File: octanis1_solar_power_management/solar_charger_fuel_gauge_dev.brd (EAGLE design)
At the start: 100 x 58.4 mm, 14 parts, among them IC1 MSP430FW42IP, U1 BQ24210_DQC_10

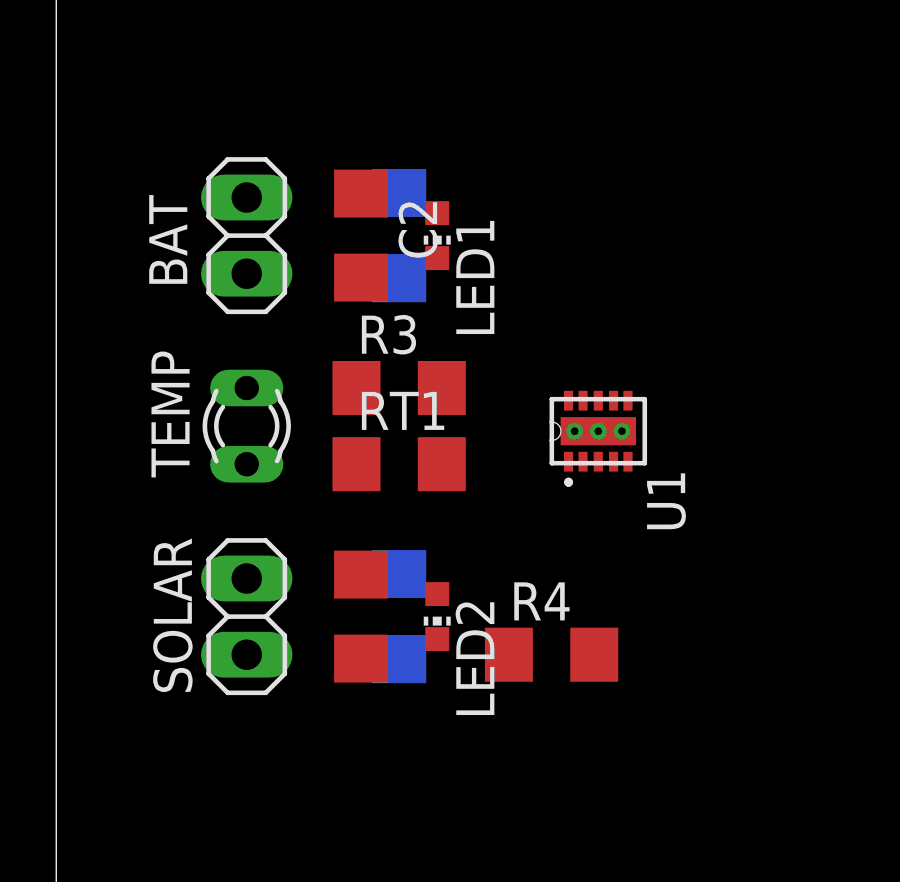
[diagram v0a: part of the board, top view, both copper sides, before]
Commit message: Completed Routing for Battery charging Part
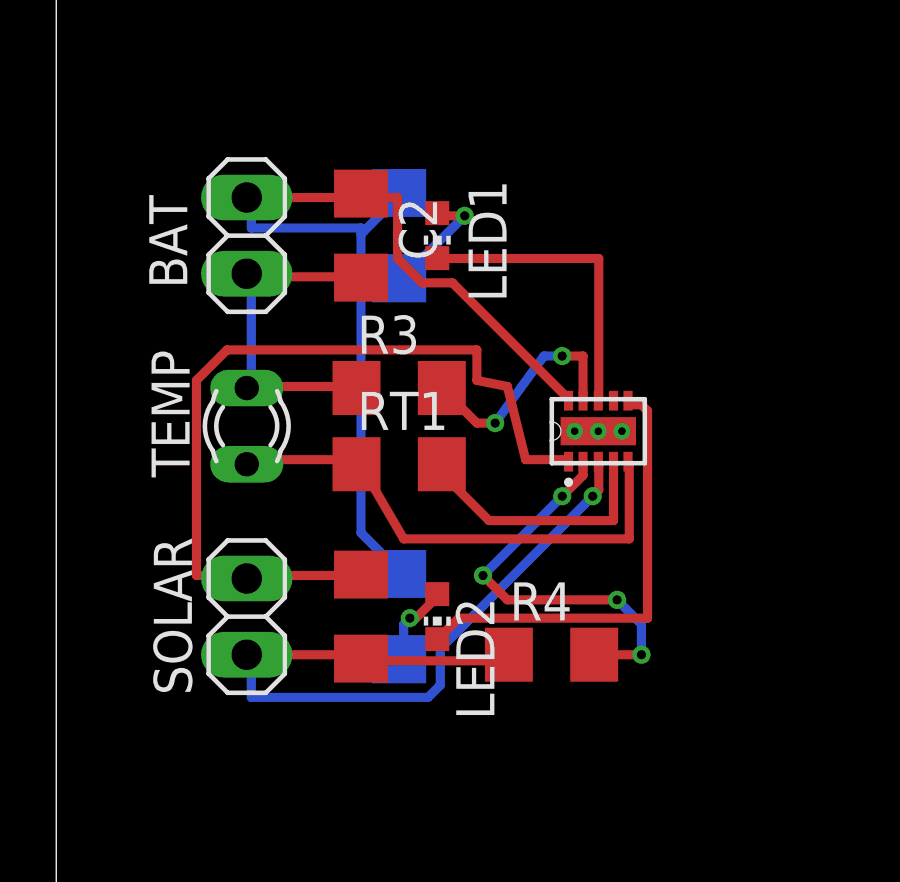
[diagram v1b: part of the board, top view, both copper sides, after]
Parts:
- U1: value BQ24210_DQC_10 -> BQ24210
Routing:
- net N$1: track 0.00 -> 33.6 mm
- net N$13: track 0.00 -> 27.9 mm
- net SOLAR: track 0.00 -> 26.7 mm, vias 0 -> 1
- net N$7: track 0.00 -> 16.9 mm
- net N$5: track 0.00 -> 15.0 mm
- net N$10: track 0.00 -> 13.7 mm, vias 0 -> 4
- net GND: track 0.00 -> 11.6 mm
- net N$4: track 0.00 -> 10.1 mm
- net N$8: track 0.00 -> 8.65 mm
- net N$6: track 0.00 -> 7.82 mm, vias 0 -> 2
- net N$2: track 0.00 -> 3.98 mm, vias 0 -> 1
- net N$3: track 0.00 -> 2.80 mm, vias 0 -> 1

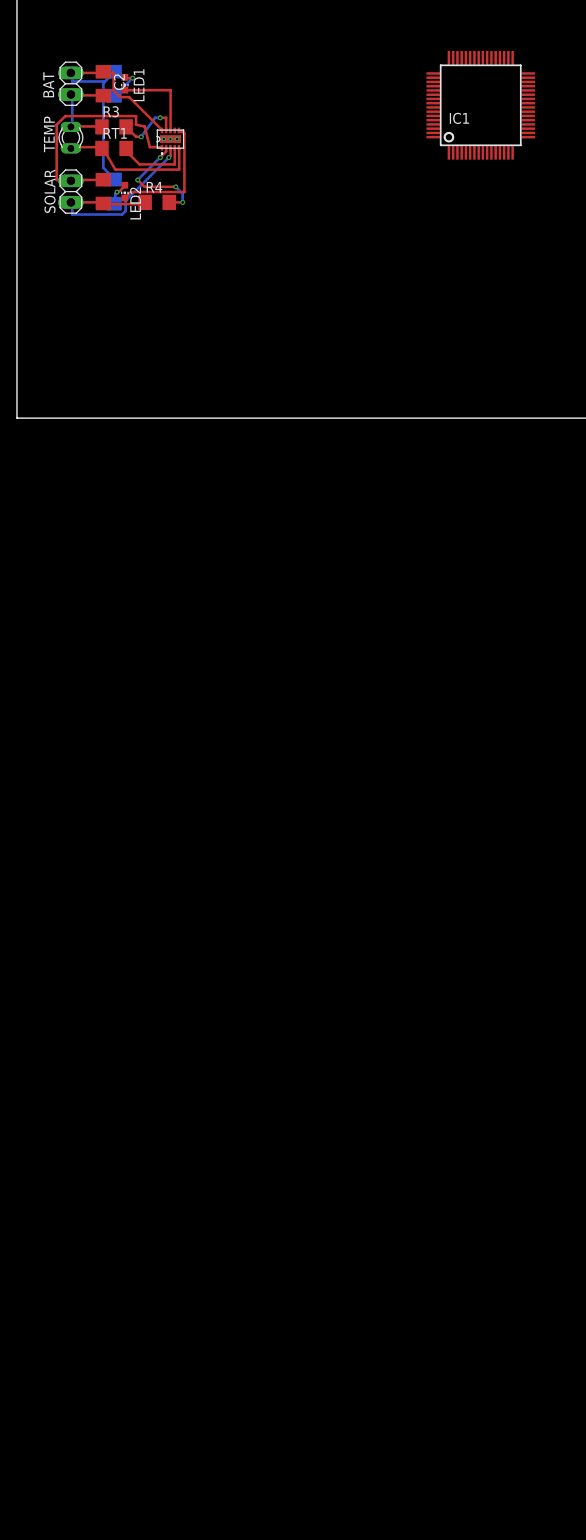
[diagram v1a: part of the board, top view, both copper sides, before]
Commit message: Added the correct MSP430 microcontroller with example circuit from LaunchPad DevBrd
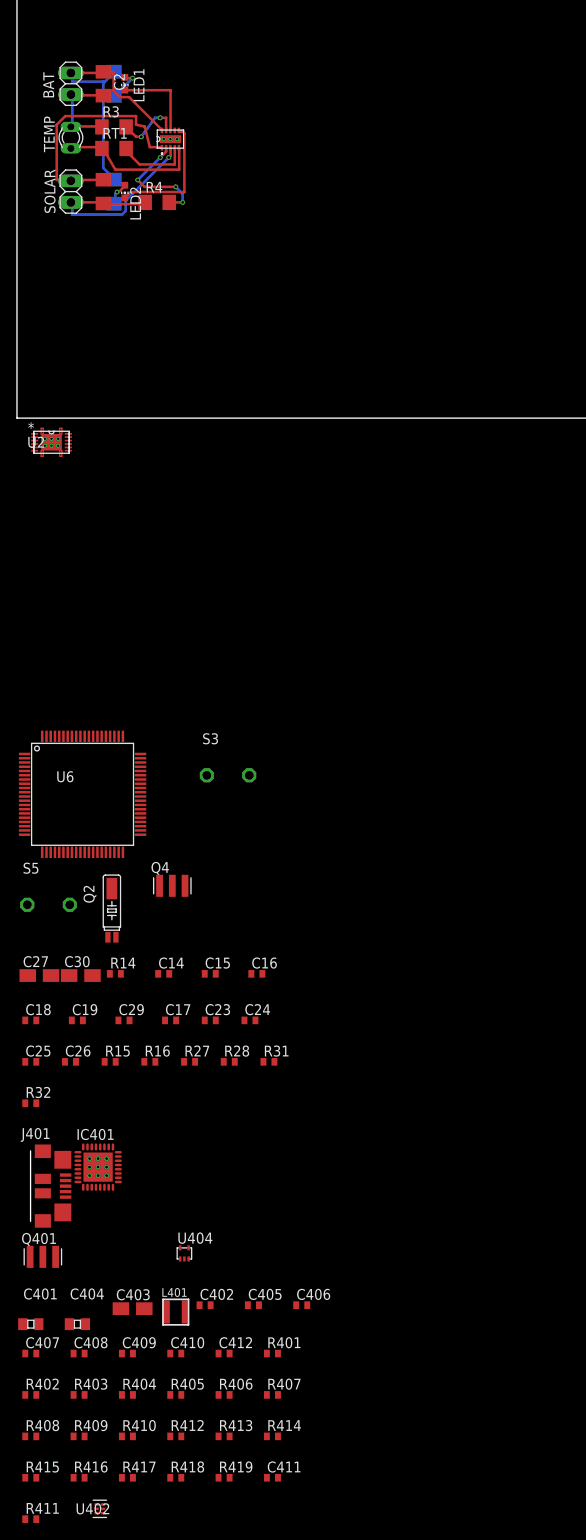
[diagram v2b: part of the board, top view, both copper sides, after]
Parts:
- removed IC1: MSP430FW42IP, texas:SQFP-S-10X10-64
- added C14, C19, C29, C402, C407, C408: 100n, rcl:C0402
- added C15, C16: 220n, rcl:C0402
- added C17: 1n, rcl:C0402
- added C18: 470n, rcl:C0402
- added C23, C24: 10p, rcl:C0402
- added C25, C26: 12p, rcl:C0402
- added C27, C403: 4u7, rcl:A/3216-18R
- added C30: 10u, rcl:A/3216-18R
- added C401, C404: 1u, CAP:CSMD0805
- added C405, C406, C409, C410, C411, C412: 22p, rcl:C0402
- added IC401: TUSB2046BIRHBIRHB, texas:RHB_S-PQFP-N32
- added J401: (no value), usb_con-update:HIROSE-ZX62R-B-5P
- added L401: 2.2uH (NR3010T2R2M), MSP-EXP430F5659:L-NR3010
- added Q2: 32.768kHz, microcrystal:MS3V-T1R
- added Q4: CSTCR4M00G15L99, murata:MURATA-FILTER_CSTCR
- added Q401: CSTCR6M00G15L99, murata:MURATA-FILTER_CSTCR
- added R14: 100R, rcl:R0402
- added R15: 1k4, rcl:R0402
- added R16: 1M, rcl:R0402
- added R27, R404: 47k, rcl:R0402
- added R28: 0R, rcl:R0402
- added R31, R32: 27R, rcl:R0402
- added R401: 33R, rcl:R0402
- added R402: 10k, rcl:R0402
- added R403, R407: 1k5, rcl:R0402
- added R405, R406, R410, R411, R416, R417: 22R, rcl:R0402
- added R408, R409, R412, R413, R414, R415, R418, R419: 15k, rcl:R0402
- added S3: RST, electricalmeter:PBTH
- added S5: BSL, electricalmeter:PBTH
- added U2: BQ27510_DRZ_12, bq27510_drz_12:DRZ12_1P95X2P45
- added U402: TPS62237DRY, tps62231dry:DRY6
- added U404: TPD2E001DRLR, Project7264:TPD2E001-DRL
- added U6: MSP430F5529IPNR, TI_MSP430_v16_intern:PN80
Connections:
- removed net AVSS: IC1.62
- removed net DVCC: IC1.1
- removed net DVSS: IC1.63
- new net !OC: IC401.10, IC401.14, IC401.18, IC401.22, R402.2
- new net !PWRON: IC401.13, IC401.17, IC401.21, IC401.9
- new net +3V3: C14.1, C19.2, C30.+, R27.2, R28.2, S5.1, U6.18, U6.50
- new net +5V: C27.+, U6.65
- new net EZFET_VBUS: C402.1, C403.+, C404.2, J401.VBUS, U402.3, U402.5, U404.1
- new net EZFET_VCC: C401.2, C407.1, IC401.25, IC401.26, IC401.3, IC401.6, IC401.8, L401.P$2, R402.1, R403.1, R404.1, U402.6
- new net HUB_DM1: R31.1, R416.2, R419.1
- new net HUB_DM2: R410.2, R415.1
- new net HUB_DP1: R32.1, R417.2, R418.1
- new net HUB_DP2: R411.2, R414.1
- new net N$14: R14.1, S5.2
- new net N$15: J401.SHIELD1, R401.1
- new net N$16: J401.D+, R405.2, U404.5
- new net N$17: J401.D-, R406.2, U404.3
- new net N$18: C406.1, IC401.2, R406.1
- new net N$19: C405.1, IC401.1, R403.2, R405.1
- new net N$20: C412.1, IC401.11, R416.1
- new net N$21: C411.1, IC401.12, R417.1
- new net N$22: C409.1, IC401.16, R411.1
- new net N$23: C410.1, IC401.15, R410.1
- new net N$24: L401.P$1, U402.2
- new net N$25: IC401.29, R407.2
- new net N$26: C408.1, IC401.4, R404.2
- new net N$27: IC401.24, R408.2
- new net N$28: IC401.23, R409.2
- new net N$29: IC401.20, R412.2
- new net N$30: IC401.19, R413.2
- new net N$31: Q401.3, R407.1
- new net N$32: IC401.30, Q401.1
- new net P1.0: U6.21
- new net P1.1: U6.22
- new net P1.2: U6.23
- new net P1.3: U6.24
- new net P1.4: U6.25
- new net P1.5: U6.26
- new net P1.6: U6.27
- new net P1.7: U6.28
- new net P2.0: U6.29
- new net P2.1: U6.30
- new net P2.2: U6.31
- new net P2.3: U6.32
- new net P2.4: U6.33
- new net P2.5: U6.34
- new net P2.6: U6.35
- new net P2.7: U6.36
- new net P3.0: U6.37
- new net P3.1: U6.38
- new net P3.2: U6.39
- new net P3.3: U6.40
- new net P3.4: U6.41
- new net P3.5: U6.42
- new net P3.6: U6.43
- new net P3.7: U6.44
- new net P4.0: U6.45
- new net P4.1: U6.46
- new net P4.2: U6.47
- new net P4.3: U6.48
- new net P4.4/UCA1TXD: U6.51
- new net P4.5/UCA1RXD: U6.52
- new net P4.7: U6.54
- new net P5.2/XT2IN: Q4.3, U6.69
- new net P5.3/XT2OUT: Q4.1, U6.70
- new net P5.4/XIN: C26.2, Q2.P2, U6.12
- new net P5.5/XOUT: C25.2, Q2.P1, U6.13
- new net P6.0: U6.77
- new net P6.1: U6.78
- new net P6.2: U6.79
- new net P6.3: U6.80
- new net P6.4: U6.1
- new net P6.5: U6.2
- new net P6.6: U6.3
- new net P6.7: U6.4
- new net P7.0: U6.5
- new net P7.4: U6.57
- new net P8.1: U6.16
- new net P8.2: U6.17
- new net REG25: U2.2
- new net REGIN: U2.3
- new net RST/SBWTDIO: C17.1, R27.1, S3.2, U6.76
- new net TARGET_DM: C24.1, R31.2, U6.64
- new net TARGET_DP: C23.1, R15.2, R32.2, U6.62
- new net TARGET_PUR: R14.2, R15.1, R16.2, U6.63
- new net TARGET_VUSB: C16.1, U6.66
- new net TEST/SBWTCK: U6.71
- new net V18: C15.1, U6.67
- new net VCC: U2.5
- new net VCORE: C18.2, U6.20
- new net VSS: U2.6
- net AVCC: now also C29.1, R28.1, U6.11; no longer IC1.64
- net EPAD: now also U2.13
- net GND: now also C14.2, C15.2, C16.2, C17.2, C18.1, C19.1, C23.2, C24.2, C25.1, C26.1, C27.-, C29.2, C30.-, C401.1, C402.2, C403.-, C404.1, C405.2, C406.2, C407.2, C408.2, C409.2, C410.2, C411.2, C412.2, IC401.27, IC401.28, IC401.31, IC401.7, J401.GND, Q2.P3, Q4.2, Q401.2, R16.1, R401.2, R408.1, R409.1, R412.1, R413.1, R414.2, R415.2, R418.2, R419.2, S3.1, U402.1, U402.4, U404.4, U6.14, U6.19, U6.49, U6.61, U6.68

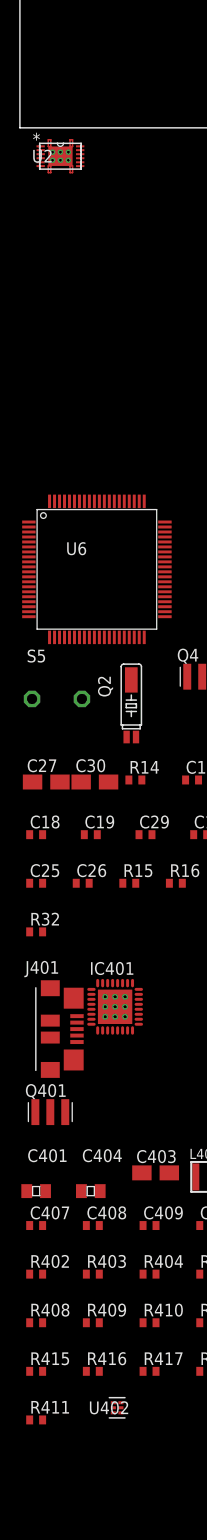
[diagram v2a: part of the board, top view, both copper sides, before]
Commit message: Added I2C
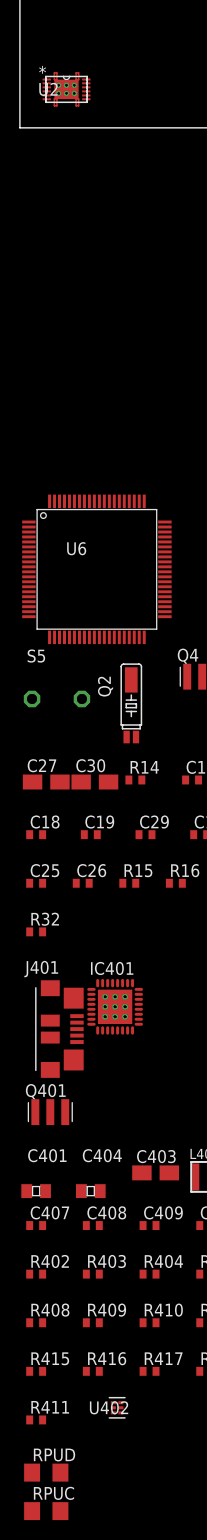
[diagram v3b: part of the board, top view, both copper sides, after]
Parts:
- added RPUC, RPUD: 10k, resistor:R1206
- moved U2 6.73 mm to (4.67, 3.86)
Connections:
- removed net P4.0: U6.45
- removed net P4.1: U6.46
- new net I2C_CLK: RPUC.1, U2.11, U6.45
- new net I2C_DATA: RPUD.1, U2.10, U6.46
- net +3V3: now also RPUC.2, RPUD.2
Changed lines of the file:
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@@
 <attribute name="VALUE" x="9.525" y="24.13" size="1.27" layer="27" rot="R90"/>
 </element>
-<element name="U2" library="bq27510_drz_12" package="DRZ12_1P95X2P45" value="BQ27510_DRZ_12" x="4.064" y="-2.8448">
-<attribute name="DATASHEETURL" value="Unknown" x="4.064" y="-2.8448" size="1.778" layer="27" display="off"/>
-<attribute name="PIN_COUNT" value="12" x="4.064" y="-2.8448" size="1.778" layer="27" display="off"/>
-<attribute name="GENERIC_PART_NUMBER" value="BQ27510" x="4.064" y="-2.8448" size="1.778" layer="27" display="off"/>
-<attribute name="DESCRIPTION" value="Unknown" x="4.064" y="-2.8448" size="1.778" layer="27" display="off"/>
-<attribute name="FAMILY_NAME" value="Unknown" x="4.064" y="-2.8448" size="1.778" layer="27" display="off"/>
-<attribute name="MANUFACTURER" value="Texas Instruments" x="4.064" y="-2.8448" size="1.778" layer="27" display="off"/>
-<attribute name="INDUSTRY_STD_PKG_TYPE" value="Unknown" x="4.064" y="-2.8448" size="1.778" layer="27" display="off"/>
-<attribute name="PACKAGE_DESIGNATOR" value="DRZ" x="4.064" y="-2.8448" size="1.778" layer="27" display="off"/>
+<element name="U2" library="bq27510_drz_12" package="DRZ12_1P95X2P45" value="BQ27510_DRZ_12" x="4.6736" y="3.8608">
+<attribute name="DATASHEETURL" value="Unknown" x="4.6736" y="3.8608" size="1.778" layer="27" display="off"/>
+<attribute name="PIN_COUNT" value="12" x="4.6736" y="3.8608" size="1.778" layer="27" display="off"/>
+<attribute name="GENERIC_PART_NUMBER" value="BQ27510" x="4.6736" y="3.8608" size="1.778" layer="27" display="off"/>
+<attribute name="DESCRIPTION" value="Unknown" x="4.6736" y="3.8608" size="1.778" layer="27" display="off"/>
+<attribute name="FAMILY_NAME" value="Unknown" x="4.6736" y="3.8608" size="1.778" layer="27" display="off"/>
+<attribute name="MANUFACTURER" value="Texas Instruments" x="4.6736" y="3.8608" size="1.778" layer="27" display="off"/>
+<attribute name="INDUSTRY_STD_PKG_TYPE" value="Unknown" x="4.6736" y="3.8608" size="1.778" layer="27" display="off"/>
+<attribute name="PACKAGE_DESIGNATOR" value="DRZ" x="4.6736" y="3.8608" size="1.778" layer="27" display="off"/>
 </element>
 <element name="C14" library="rcl" package="C0402" value="100n" x="17.272" y="-65.4304"/>
@@
 <element name="R413" library="rcl" package="R0402" value="15k" x="24.384" y="-119.888"/>
 <element name="R412" library="rcl" package="R0402" value="15k" x="18.6944" y="-119.888"/>
+<element name="RPUD" library="resistor" package="R1206" value="10k" x="2.6416" y="-134.9248"/>
+<element name="RPUC" library="resistor" package="R1206" value="10k" x="2.6416" y="-138.7856"/>
 </elements>
 <signals>
@@
 <contactref element="U1" pad="11"/>
 <contactref element="U2" pad="13"/>
-<wire x1="4.064" y1="-2.8448" x2="18.0681" y2="32.8508" width="0" layer="19" extent="1-1"/>
+<wire x1="4.6736" y1="3.8608" x2="18.0681" y2="32.8508" width="0" layer="19" extent="1-1"/>
 </signal>
 <signal name="GND">
@@
 <contactref element="U6" pad="44"/>
 </signal>
-<signal name="P4.0">
+<signal name="I2C_CLK">
 <contactref element="U6" pad="45"/>
+<contactref element="RPUC" pad="1"/>
+<contactref element="U2" pad="11"/>
+<wire x1="14.5466" y1="-47.0476" x2="1.2196" y2="-138.7856" width="0" layer="19" extent="1-1"/>
+<wire x1="6.6548" y1="4.4704" x2="14.5466" y2="-47.0476" width="0" layer="19" extent="1-1"/>
 </signal>
 <signal name="P6.5">
@@
 <contactref element="U6" pad="43"/>
 </signal>
-<signal name="P4.1">
+<signal name="I2C_DATA">
 <contactref element="U6" pad="46"/>
+<contactref element="RPUD" pad="1"/>
+<contactref element="U2" pad="10"/>
+<wire x1="14.5466" y1="-46.5476" x2="1.2196" y2="-134.9248" width="0" layer="19" extent="1-1"/>
+<wire x1="6.6548" y1="4.064" x2="14.5466" y2="-46.5476" width="0" layer="19" extent="1-1"/>
 </signal>
 <signal name="P3.0">
@@
 <contactref element="C14" pad="1"/>
 <contactref element="U6" pad="50"/>
-<wire x1="8.8934" y1="-65.6336" x2="7.762" y2="-70.9168" width="0" layer="19" extent="1-1"/>
-<wire x1="16.622" y1="-65.4304" x2="8.8934" y2="-65.6336" width="0" layer="19" extent="1-1"/>
-<wire x1="20.97" y1="-75.7936" x2="16.622" y2="-65.4304" width="0" layer="19" extent="1-1"/>
+<contactref element="RPUD" pad="2"/>
+<contactref element="RPUC" pad="2"/>
+<wire x1="4.0636" y1="-134.9248" x2="4.0636" y2="-138.7856" width="0" layer="19" extent="1-1"/>
+<wire x1="20.97" y1="-75.7936" x2="4.0636" y2="-134.9248" width="0" layer="19" extent="1-1"/>
 <wire x1="25.6436" y1="-75.7936" x2="20.97" y2="-75.7936" width="0" layer="19" extent="1-1"/>
+<wire x1="16.622" y1="-65.4304" x2="20.97" y2="-75.7936" width="0" layer="19" extent="1-1"/>
+<wire x1="8.8934" y1="-65.6336" x2="16.622" y2="-65.4304" width="0" layer="19" extent="1-1"/>
+<wire x1="7.762" y1="-70.9168" x2="8.8934" y2="-65.6336" width="0" layer="19" extent="1-1"/>
 <wire x1="1.218" y1="-57.3018" x2="8.8934" y2="-65.6336" width="0" layer="19" extent="1-1"/>
 <wire x1="0.8966" y1="-48.0476" x2="1.218" y2="-57.3018" width="0" layer="19" extent="1-1"/>

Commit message: Added Fuel Gauge Circuit in Schematic
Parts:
- removed TEMP: (no value), ptc-ntc:P640
- added C3: 33nF, rcl:C1206
- added C4, C6, C7, C8, C9: 0.1uF, rcl:C1206
- added C5: 0.47uF, rcl:C1206
- added R5, R6: (no value), resistor:R1206
- added R7, R8: 100, resistor:R1206
- added RSBAT: 0.01, resistor:R1206
- added RT2: 1k, resistor:R1206
- added TEMP1, TEMP2: 103AT, varistor:RS-2,5
- moved U2 45.5 mm to (13.4, 48.6)
- renumbered BAT to BATTERY
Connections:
- removed net EPAD: U1.11, U2.13
- removed net REG25: U2.2
- removed net REGIN: U2.3
- removed net VCC: U2.5
- removed net VSS: U2.6
- new net BAT+: BATTERY.1, C2.1, C6.1, R1.2, R2.2, U1.10, U2.3, U2.4
- new net BAT-: BATTERY.2, R8.1, RSBAT.1
- new net N$33: R5.1, RT2.2, TEMP2.1
- new net N$34: C4.1, RT2.1, U2.9
- new net N$35: C5.1, R6.2, U2.2, U2.5
- new net N$36: C7.1, C9.1, R7.2, U2.8
- new net N$38: C8.2, C9.2, R8.2, U2.7
- net GND: now also C3.2, C4.2, C5.2, C6.2, C7.2, C8.1, R7.1, RSBAT.2, TEMP1.1, TEMP2.2, U1.11, U2.13, U2.6; no longer BATTERY.2, TEMP.1
- net N$1: now also C3.1, R5.2, R6.1, U2.1; no longer BATTERY.1, C2.1, R1.2, R2.2, U1.10
- net N$7: now also TEMP1.2; no longer TEMP.2
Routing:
- net N$1: track 33.6 -> 0.00 mm
- net BAT+: track 0.00 -> 33.6 mm
- net GND: track 11.6 -> 7.21 mm
- net BAT-: track 0.00 -> 3.84 mm

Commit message: Renamed and placed Parts for fuel gauge part of circuit
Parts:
- removed C3: 33nF, rcl:C1206
- removed C4, C6, C7, C8, C9: 0.1uF, rcl:C1206
- removed C5: 0.47uF, rcl:C1206
- removed R5, R6: (no value), resistor:R1206
- removed R7, R8: 100, resistor:R1206
- removed RT2: 1k, resistor:R1206
- added CG1, CG3, CG6, CG7, CG8: 0.1uF, rcl:C1206
- added CG2: 33nF, rcl:C1206
- added CG4: 0.47uF, rcl:C1206
- added RG1, RG2: (no value), resistor:R1206
- added RG3: 1k, resistor:R1206
- added RG5, RG6: 100, resistor:R1206
- moved RSBAT 204.2 mm to (5.69, 52.6), turned to 90 degrees
- moved TEMP2 190.4 mm to (6.30, 43.9), turned to 90 degrees
- moved U2 7.66 mm to (20.5, 45.7)
- moved TEMP1 1.22 mm to (6.35, 31.8)
- moved BATTERY 1.22 mm to (6.35, 38.2)
- moved C1 1.22 mm to (10.2, 25.5)
- moved C2 1.22 mm to (10.2, 38.2)
- moved LED1 1.22 mm to (12.7, 38.2)
- moved LED2 1.22 mm to (12.7, 25.5)
- moved R1 1.22 mm to (11.4, 38.2)
- moved R2 1.22 mm to (11.4, 25.5)
- moved R3 1.22 mm to (11.4, 33.1)
- moved RT1 1.22 mm to (11.4, 30.5)
- moved SOLAR 1.22 mm to (6.35, 25.5)
- moved U1 1.22 mm to (18.1, 31.6)
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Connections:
- net BAT+: now also CG3.1; no longer C6.1
- net BAT-: now also RG6.1; no longer R8.1
- net GND: now also CG1.2, CG2.2, CG3.2, CG4.2, CG7.2, CG8.1, RG5.1; no longer C3.2, C4.2, C5.2, C6.2, C7.2, C8.1, R7.1
- net N$1: now also CG2.1, RG1.1, RG2.2; no longer C3.1, R5.2, R6.1
- net N$33: now also RG2.1, RG3.2; no longer R5.1, RT2.2
- net N$34: now also CG1.1, RG3.1; no longer C4.1, RT2.1
- net N$35: now also CG4.1, RG1.2; no longer C5.1, R6.2
- net N$36: now also CG6.1, CG7.1, RG5.2; no longer C7.1, C9.1, R7.2
- net N$38: now also CG6.2, CG8.2, RG6.2; no longer C8.2, C9.2, R8.2
